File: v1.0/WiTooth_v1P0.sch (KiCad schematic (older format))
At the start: 47 parts, among them P1 USB_A_MALE, P4 CONN_01X20, P5 CONN_01X20, Q1 Q_NPN_EBC, Q2 Q_NPN_EBC, SW1 RESET, SW2 BOOT, SW3 USER_SW, U1 AMS1117-3V3, U2 CP2102, U3 ESP-32_WROOM32_Rectangle, Y1 Crystal

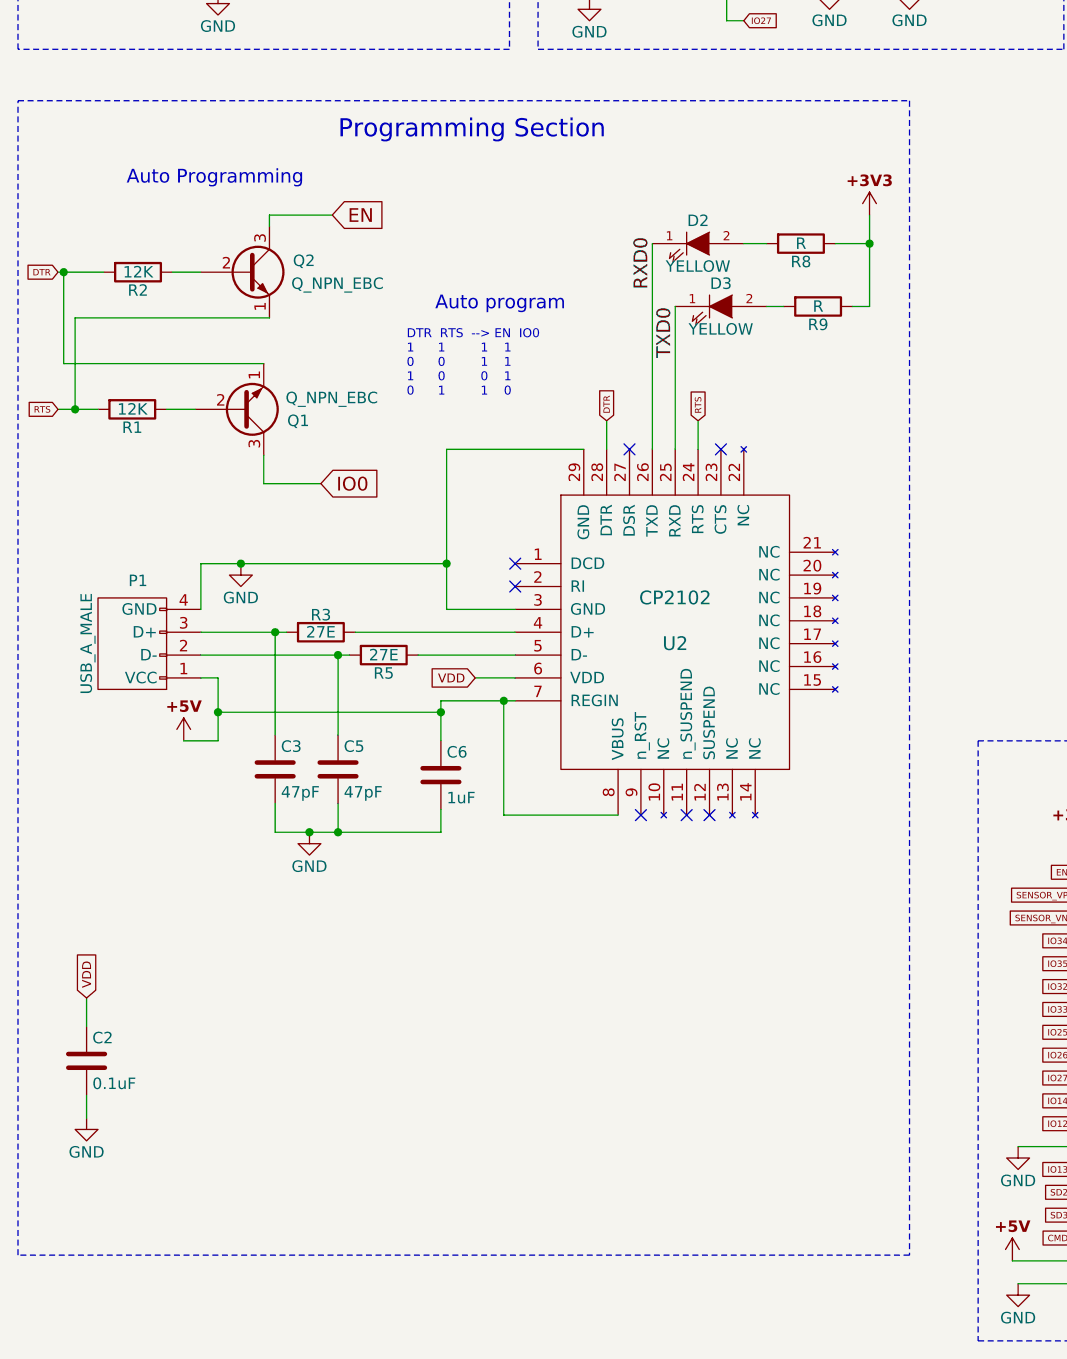
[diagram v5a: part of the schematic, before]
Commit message: BOM generated and Routing Done
- Bom generated
- Routing Completed
- Silk Screen Added
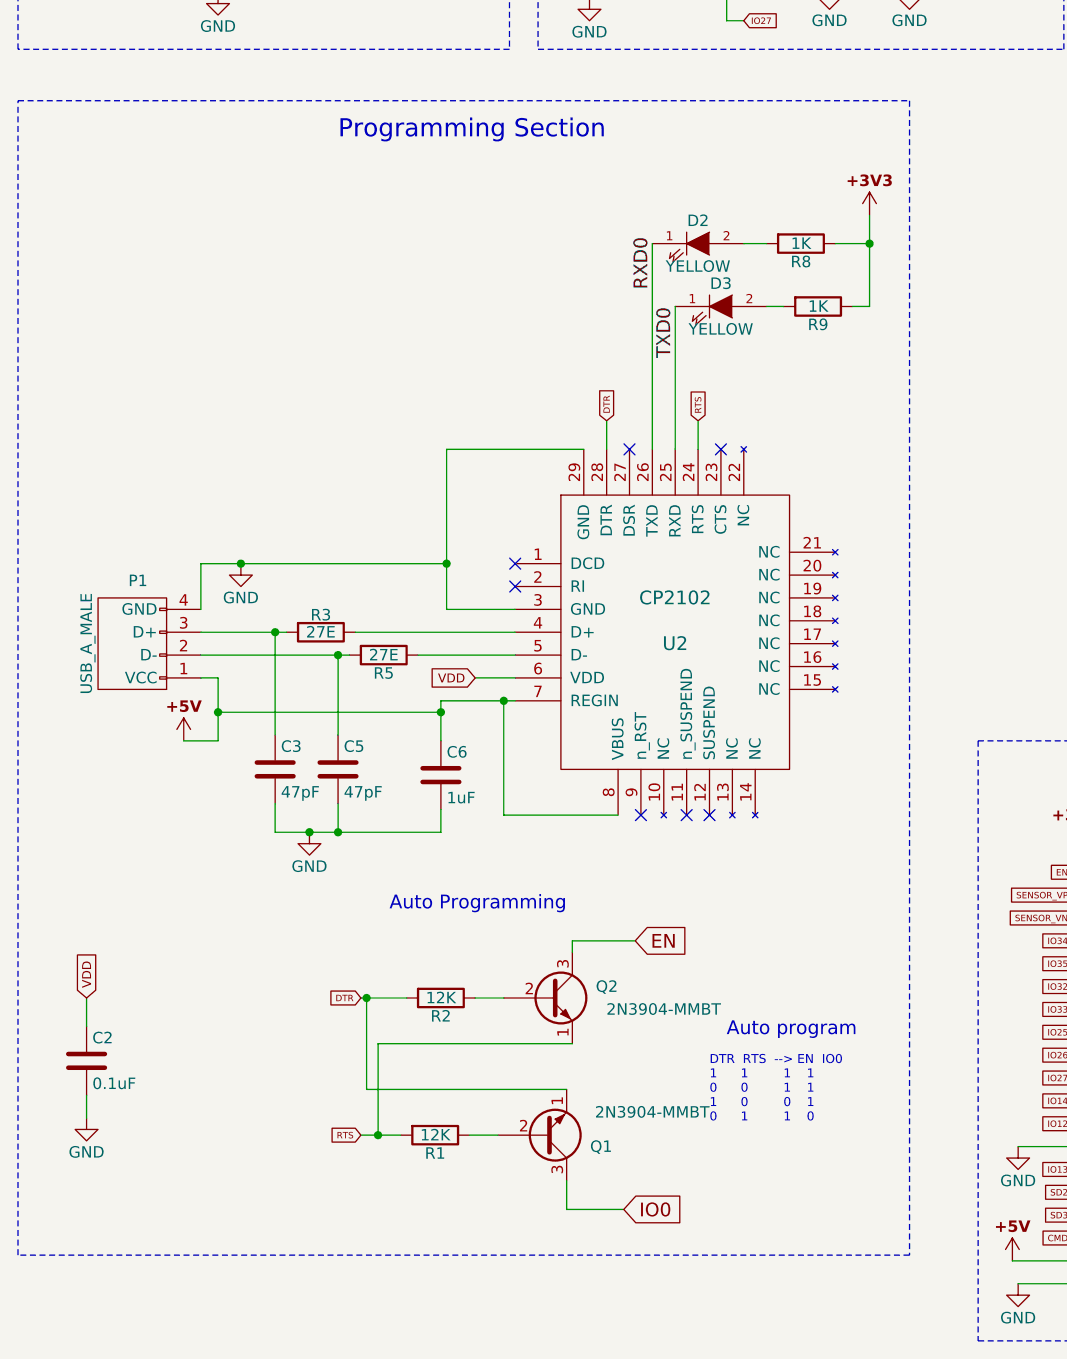
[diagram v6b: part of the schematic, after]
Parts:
- Q1, Q2: value Q_NPN_EBC -> 2N3904-MMBT
- R8, R9: value R -> 1K
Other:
- moved on the sheet: Q1, Q2, R1, R2
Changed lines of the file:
@@
 LIBS:crystal-new
 LIBS:usb_a_male_pcb
+LIBS:4n35_opto
+LIBS:24MHz
+LIBS:0850bm14e0016
+LIBS:2450BM14G0011
+LIBS:antenna_2.4GHz
+LIBS:cc1310_7x7
+LIBS:cc1310_7x7_new
+LIBS:cc2650
+LIBS:cc2650_7x7
+LIBS:connectors
+LIBS:crystal_24MHz
+LIBS:df08s1_bridge_rec-ic
+LIBS:edge_sma
+LIBS:esp-12e
+LIBS:esp-32_wroom32_Exact
+LIBS:henlv_5v_2a
+LIBS:henlv-ac220s3_3dcs-3w
+LIBS:HM-10
+LIBS:ic-cpu
+LIBS:ic-io
+LIBS:ic-misc
+LIBS:ic-power
+LIBS:inductor
+LIBS:inductor_L
+LIBS:lp5907_ldo_250ma
+LIBS:ltr-303als
+LIBS:Micro_USB_B
+LIBS:passive
+LIBS:PROBE
+LIBS:RFM_module
+LIBS:sfm-110-02-s-d-a-k-tr
+LIBS:si7006
+LIBS:switch_dpdt
+LIBS:switch_spdt
+LIBS:switches
+LIBS:tps782
+LIBS:tps63051
+LIBS:triac_board
+LIBS:vbus053az
+LIBS:xbee
 LIBS:WiTooth_v1P0-cache
 EELAYER 25 0
@@
 encoding utf-8
 Sheet 1 1
-Title ""
+Title "WiTooth"
 Date ""
 Rev "v1.0"
@@
 P 4025 3225
 F 0 "R9" V 4105 3225 50  0000 C CNN
-F 1 "R" V 4025 3225 50  0000 C CNN
+F 1 "1K" V 4025 3225 50  0000 C CNN
 F 2 "Resistors_SMD:R_0805_HandSoldering" V 3955 3225 50  0001 C CNN
 F 3 "" H 4025 3225 50  0000 C CNN
@@
 P 3950 2950
 F 0 "R8" V 4030 2950 50  0000 C CNN
-F 1 "R" V 3950 2950 50  0000 C CNN
+F 1 "1K" V 3950 2950 50  0000 C CNN
 F 2 "Resistors_SMD:R_0805_HandSoldering" V 3880 2950 50  0001 C CNN
 F 3 "" H 3950 2950 50  0000 C CNN
@@
 	1    0    0    -1
 $EndComp
-Text Notes 1000 2700 0    60   ~ 0
+Text Notes 2150 5875 0    60   ~ 0
 Auto Programming
-Text GLabel 700  3075 0    28   Input ~ 0
+Text GLabel 2025 6250 0    28   Input ~ 0
 DTR
 $Comp
 L R R2
 U 1 1 589A1209
-P 1050 3075
-F 0 "R2" V 1130 3075 50  0000 C CNN
-F 1 "12K" V 1050 3075 50  0000 C CNN
-F 2 "Resistors_SMD:R_0805_HandSoldering" V 980 3075 50  0001 C CNN
-F 3 "" H 1050 3075 50  0000 C CNN
-	1    1050 3075
+P 2375 6250
+F 0 "R2" V 2455 6250 50  0000 C CNN
+F 1 "12K" V 2375 6250 50  0000 C CNN
+F 2 "Resistors_SMD:R_0805_HandSoldering" V 2305 6250 50  0001 C CNN
+F 3 "" H 2375 6250 50  0000 C CNN
+	1    2375 6250
 	0    1    1    0
 $EndComp
@@
 L Q_NPN_EBC Q2
 U 1 1 589A127B
-P 1525 3075
-F 0 "Q2" H 1825 3125 50  0000 R CNN
-F 1 "Q_NPN_EBC" H 2125 3025 50  0000 R CNN
-F 2 "TO_SOT_Packages_SMD:SOT-23_Handsoldering" H 1725 3175 50  0001 C CNN
-F 3 "" H 1525 3075 50  0000 C CNN
-	1    1525 3075
+P 2850 6250
+F 0 "Q2" H 3150 6300 50  0000 R CNN
+F 1 "2N3904-MMBT" H 3600 6200 50  0000 R CNN
+F 2 "TO_SOT_Packages_SMD:SOT-23_Handsoldering" H 3050 6350 50  0001 C CNN
+F 3 "" H 2850 6250 50  0000 C CNN
+	1    2850 6250
 	1    0    0    -1
 $EndComp
@@
 L R R1
 U 1 1 589A13C9
-P 1025 3675
-F 0 "R1" V 1105 3675 50  0000 C CNN
-F 1 "12K" V 1025 3675 50  0000 C CNN
-F 2 "Resistors_SMD:R_0805_HandSoldering" V 955 3675 50  0001 C CNN
-F 3 "" H 1025 3675 50  0000 C CNN
-	1    1025 3675
+P 2350 6850
+F 0 "R1" V 2430 6850 50  0000 C CNN
+F 1 "12K" V 2350 6850 50  0000 C CNN
+F 2 "Resistors_SMD:R_0805_HandSoldering" V 2280 6850 50  0001 C CNN
+F 3 "" H 2350 6850 50  0000 C CNN
+	1    2350 6850
 	0    1    1    0
 $EndComp
@@
 L Q_NPN_EBC Q1
 U 1 1 589A13CF
-P 1500 3675
-F 0 "Q1" H 1800 3725 50  0000 R CNN
-F 1 "Q_NPN_EBC" H 2100 3625 50  0000 R CNN
-F 2 "TO_SOT_Packages_SMD:SOT-23_Handsoldering" H 1700 3775 50  0001 C CNN
-F 3 "" H 1500 3675 50  0000 C CNN
-	1    1500 3675
+P 2825 6850
+F 0 "Q1" H 3125 6900 50  0000 R CNN
+F 1 "2N3904-MMBT" H 3550 6750 50  0000 R CNN
+F 2 "TO_SOT_Packages_SMD:SOT-23_Handsoldering" H 3025 6950 50  0001 C CNN
+F 3 "" H 2825 6850 50  0000 C CNN
+	1    2825 6850
 	1    0    0    1
 $EndComp
-Text GLabel 700  3675 0    28   Input ~ 0
+Text GLabel 2025 6850 0    28   Input ~ 0
 RTS
-Text GLabel 1850 4000 2    60   Input ~ 0
+Text GLabel 3175 7175 2    60   Input ~ 0
 IO0
-Text GLabel 1900 2825 2    60   Input ~ 0
+Text GLabel 3225 6000 2    60   Input ~ 0
 EN
-Text Notes 2350 3250 0    60   ~ 0
+Text Notes 3625 6425 0    60   ~ 0
 Auto program
-Text Notes 2225 3625 0    39   ~ 0
+Text Notes 3550 6800 0    39   ~ 0
 DTR  RTS  --> EN  IO0\n1      1         1    1\n0      0         1    1\n1      0         0    1\n0      1         1    0
 $Comp
@@
 $EndComp
 $Comp
-L GND #PWR027
+L GND #PWR025
 U 1 1 58978B34
 P 3025 1875
-F 0 "#PWR027" H 3025 1625 50  0001 C CNN
+F 0 "#PWR025" H 3025 1625 50  0001 C CNN
 F 1 "GND" H 3025 1725 50  0000 C CNN
 F 2 "" H 3025 1875 50  0000 C CNN
@@
 $EndComp
 $Comp
-L +3V3 #PWR028
+L +3V3 #PWR026
 U 1 1 589E8561
 P 7325 1175
-F 0 "#PWR028" H 7325 1025 50  0001 C CNN
+F 0 "#PWR026" H 7325 1025 50  0001 C CNN
 F 1 "+3V3" H 7325 1325 50  0001 C CNN
 F 2 "" H 7325 1175 50  0000 C CNN
@@
 	825  6250 825  6375
 Wire Wire Line
-	700  3075 900  3075
-Wire Wire Line
-	1200 3075 1325 3075
-Wire Wire Line
-	700  3675 875  3675
-Wire Wire Line
-	1175 3675 1300 3675
-Wire Wire Line
-	1600 3475 725  3475
-Wire Wire Line
-	725  3475 725  3075
-Connection ~ 725  3075
-Wire Wire Line
-	1625 3275 775  3275
-Wire Wire Line
-	775  3275 775  3675
-Connection ~ 775  3675
-Wire Wire Line
-	1600 3875 1600 4000
-Wire Wire Line
-	1600 4000 1850 4000
-Wire Wire Line
-	1900 2825 1625 2825
-Wire Wire Line
-	1625 2825 1625 2875
+	2025 6250 2225 6250
+Wire Wire Line
+	2525 6250 2650 6250
+Wire Wire Line
+	2025 6850 2200 6850
+Wire Wire Line
+	2500 6850 2625 6850
+Wire Wire Line
+	2925 6650 2050 6650
+Wire Wire Line
+	2050 6650 2050 6250
+Connection ~ 2050 6250
+Wire Wire Line
+	2950 6450 2100 6450
+Wire Wire Line
+	2100 6450 2100 6850
+Connection ~ 2100 6850
+Wire Wire Line
+	2925 7050 2925 7175
+Wire Wire Line
+	2925 7175 3175 7175
+Wire Wire Line
+	3225 6000 2950 6000
+Wire Wire Line
+	2950 6000 2950 6050
 Wire Wire Line
 	7200 3475 7200 3575
